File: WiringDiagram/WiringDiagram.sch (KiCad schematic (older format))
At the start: 0 parts

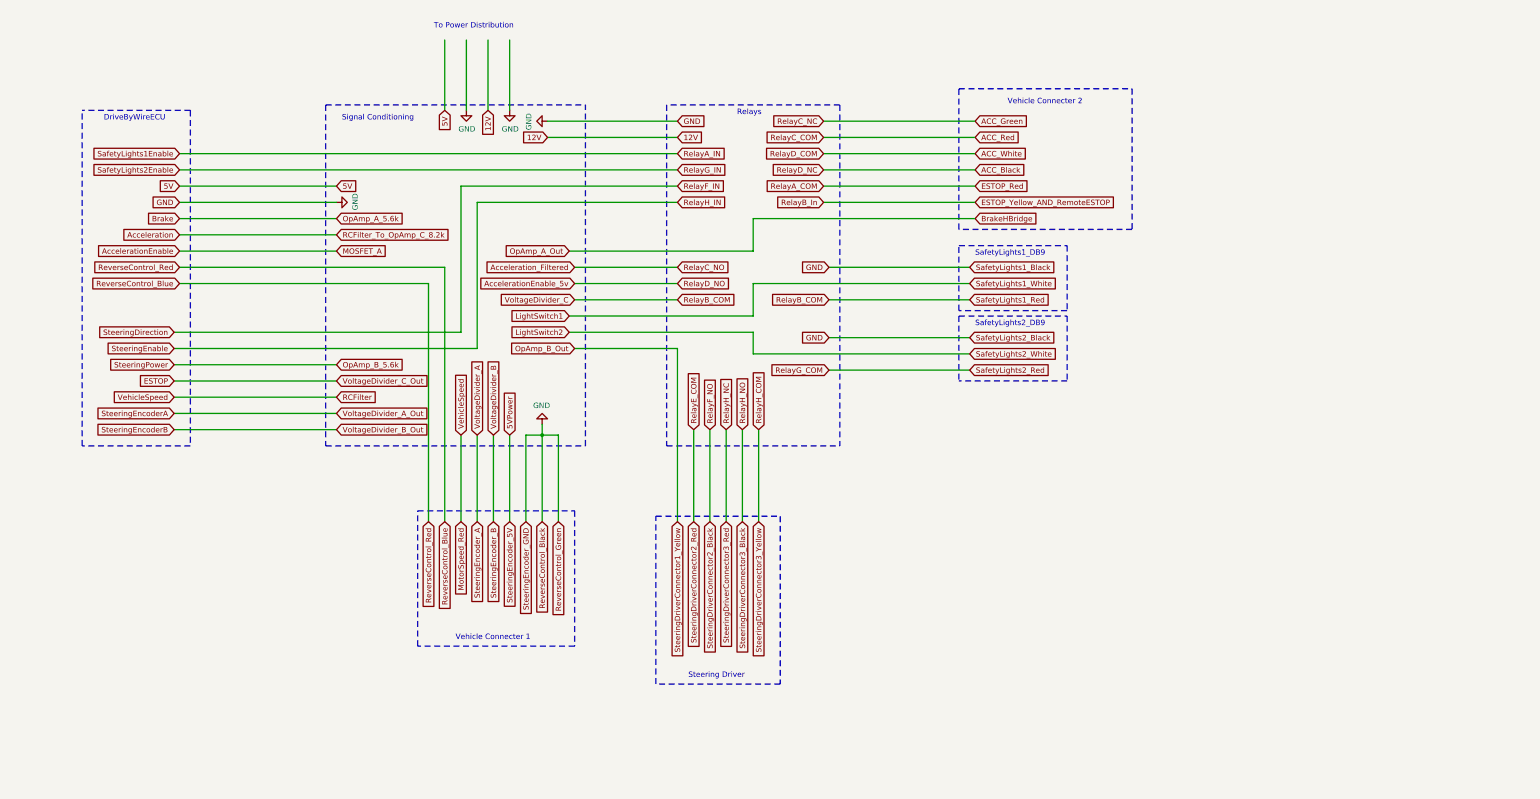
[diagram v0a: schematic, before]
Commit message: Finishes pinouts and moves them to the Wiring Daigram
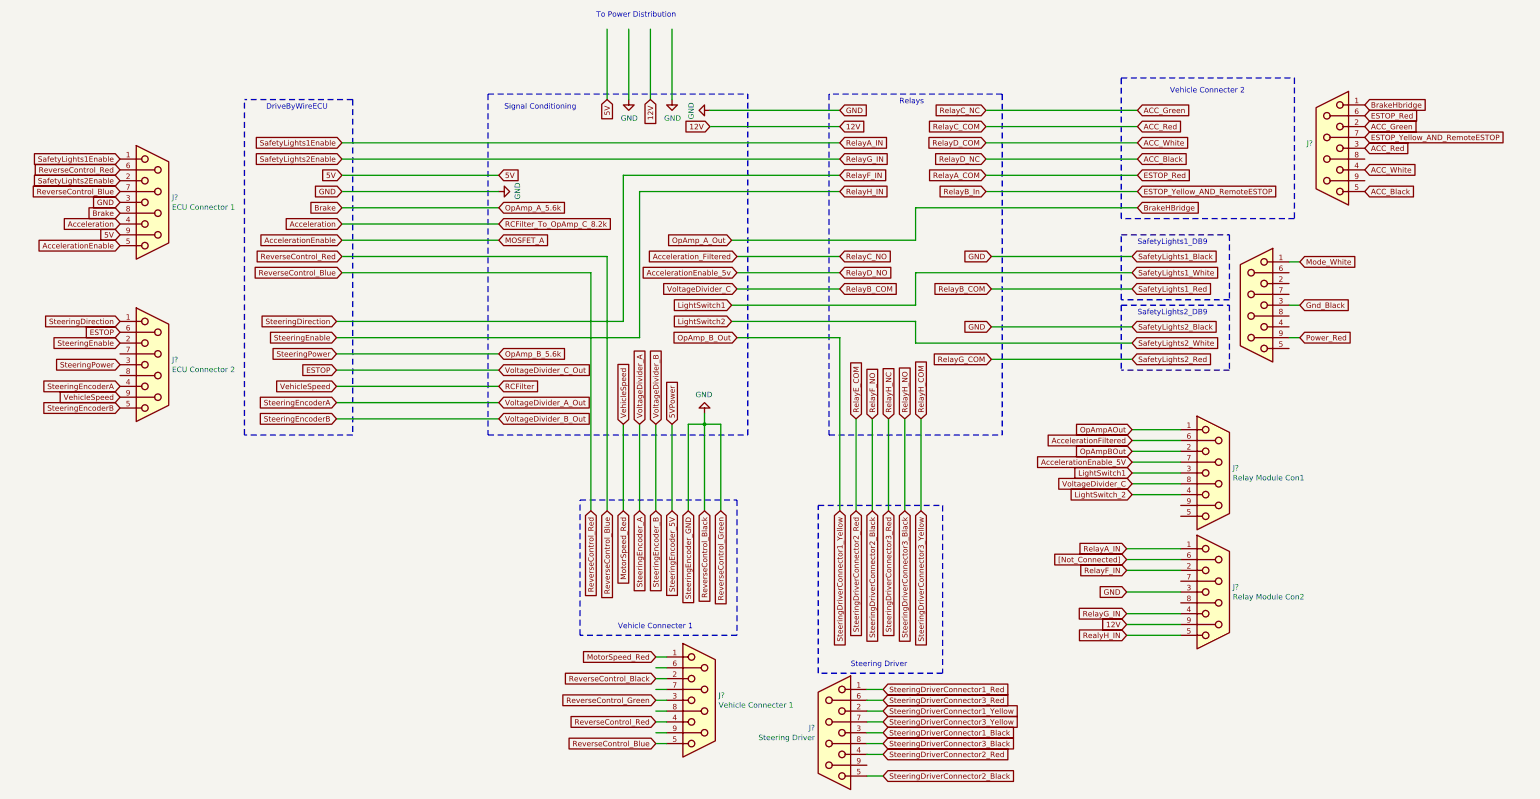
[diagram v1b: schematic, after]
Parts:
- added J1&?: SafetyLights, symbol Connector:DB9_Female
- added J?: Steering Driver, symbol Connector:DB9_Female
- added J?: Vehicle Connecter 1, symbol Connector:DB9_Female
- added J?: Relay Module Con2, symbol Connector:DB9_Female
- added J?: Relay Module Con1, symbol Connector:DB9_Female
- added J?: Vehicle Connnector 2, symbol Connector:DB9_Female
- added J?: ECU Connector 1, symbol Connector:DB9_Female
- added J?: ECU Connector 2, symbol Connector:DB9_Female
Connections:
- net labels added: AccelerationEnable_5V, AccelerationFiltered, BrakeHbridge, Gnd_Black, LightSwitch_2, Mode_White, OpAmpAOut, OpAmpBOut, Power_Red, RealyH_IN, SteeringDriverConnector1_Black, SteeringDriverConnector1_Red, [Not_Connected]
- wire segments 67 -> 101

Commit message: Encoder Pins Added to VC1 & VC2 Pins were rearranged
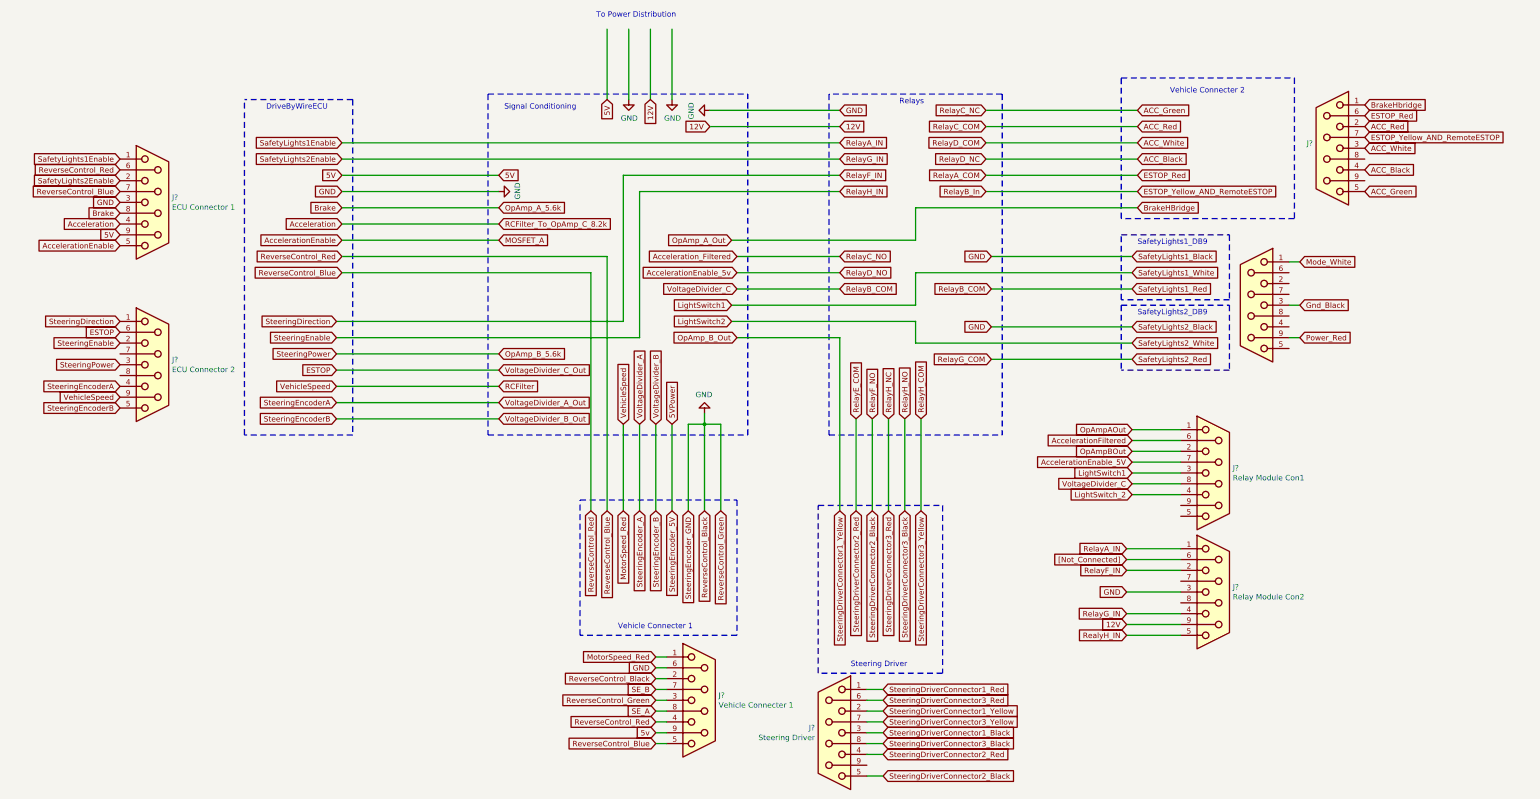
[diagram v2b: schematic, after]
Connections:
- net labels added: 5v, SE_A, SE_B
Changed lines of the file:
@@
 Wire Wire Line
 	7350 3650 8300 3650
-Text GLabel 11050 2450 2    50   Input ~ 0
-BrakeHBridge
 Text GLabel 7300 2750 0    50   Input ~ 0
 OpAmp_A_Out
@@
 Text GLabel 13150 1600 2    50   Input ~ 0
 ESTOP_Red
+Text GLabel 13150 2300 2    50   Input ~ 0
+ACC_Green
 Text GLabel 13150 1700 2    50   Input ~ 0
-ACC_Green
+ACC_Red
 Text GLabel 13150 1900 2    50   Input ~ 0
-ACC_Red
+ACC_White
 Text GLabel 13150 2100 2    50   Input ~ 0
-ACC_White
-Text GLabel 13150 2300 2    50   Input ~ 0
 ACC_Black
 Text GLabel 13150 1800 2    50   Input ~ 0
@@
 Text GLabel 1650 4200 0    50   Input ~ 0
 VehicleSpeed
+Text GLabel 11050 2450 2    50   Input ~ 0
+BrakeHBridge
+Text GLabel 6600 6700 0    50   Input ~ 0
+GND
+Text GLabel 6600 6900 0    50   Input ~ 0
+SE_B
+Text GLabel 6600 7100 0    50   Input ~ 0
+SE_A
+Text GLabel 6600 7300 0    50   Input ~ 0
+5v
 $EndSCHEMATC

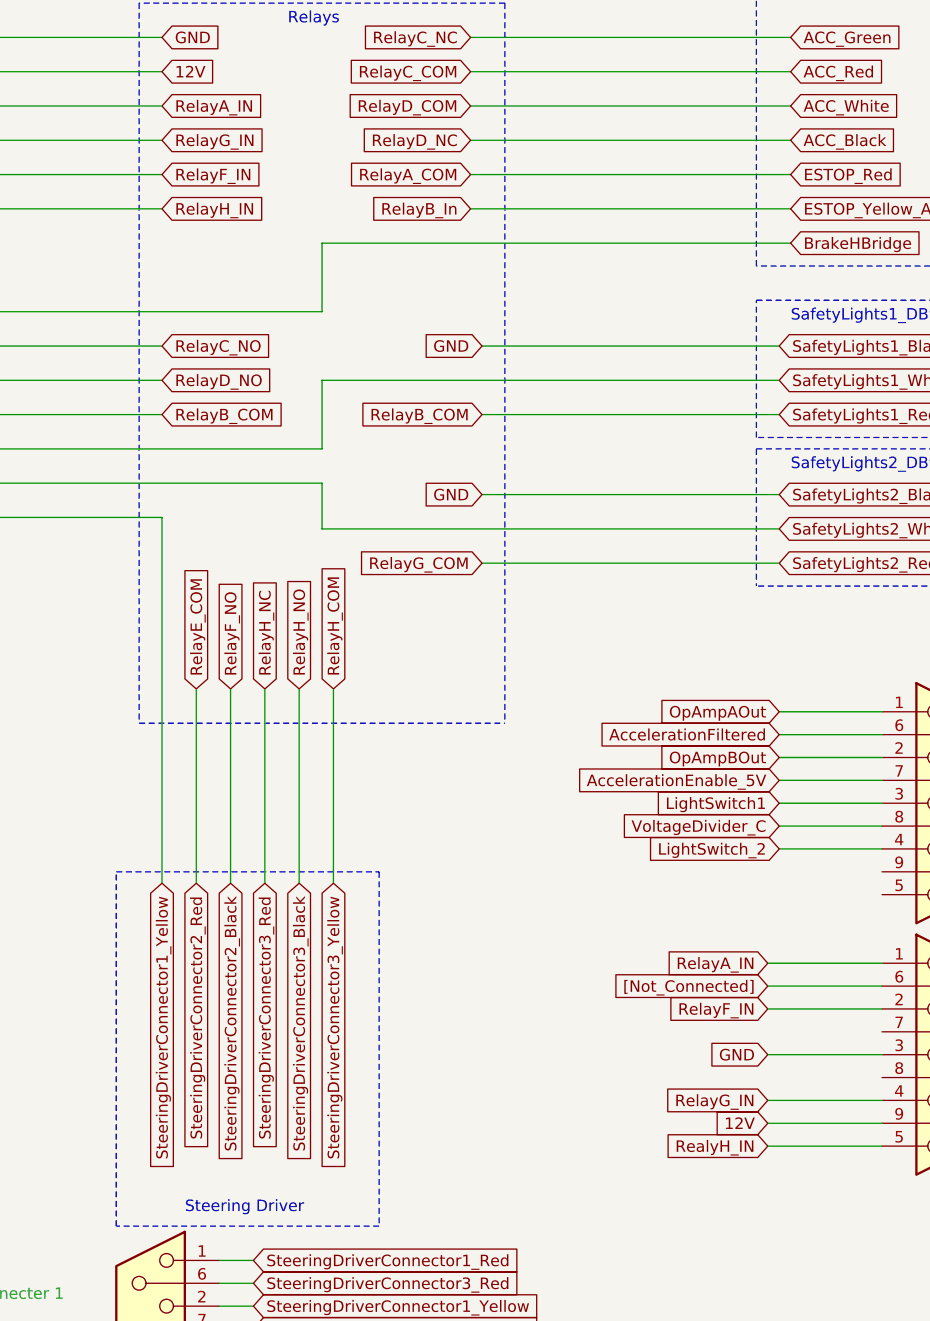
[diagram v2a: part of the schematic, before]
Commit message: Fixes relay wiring mismatch
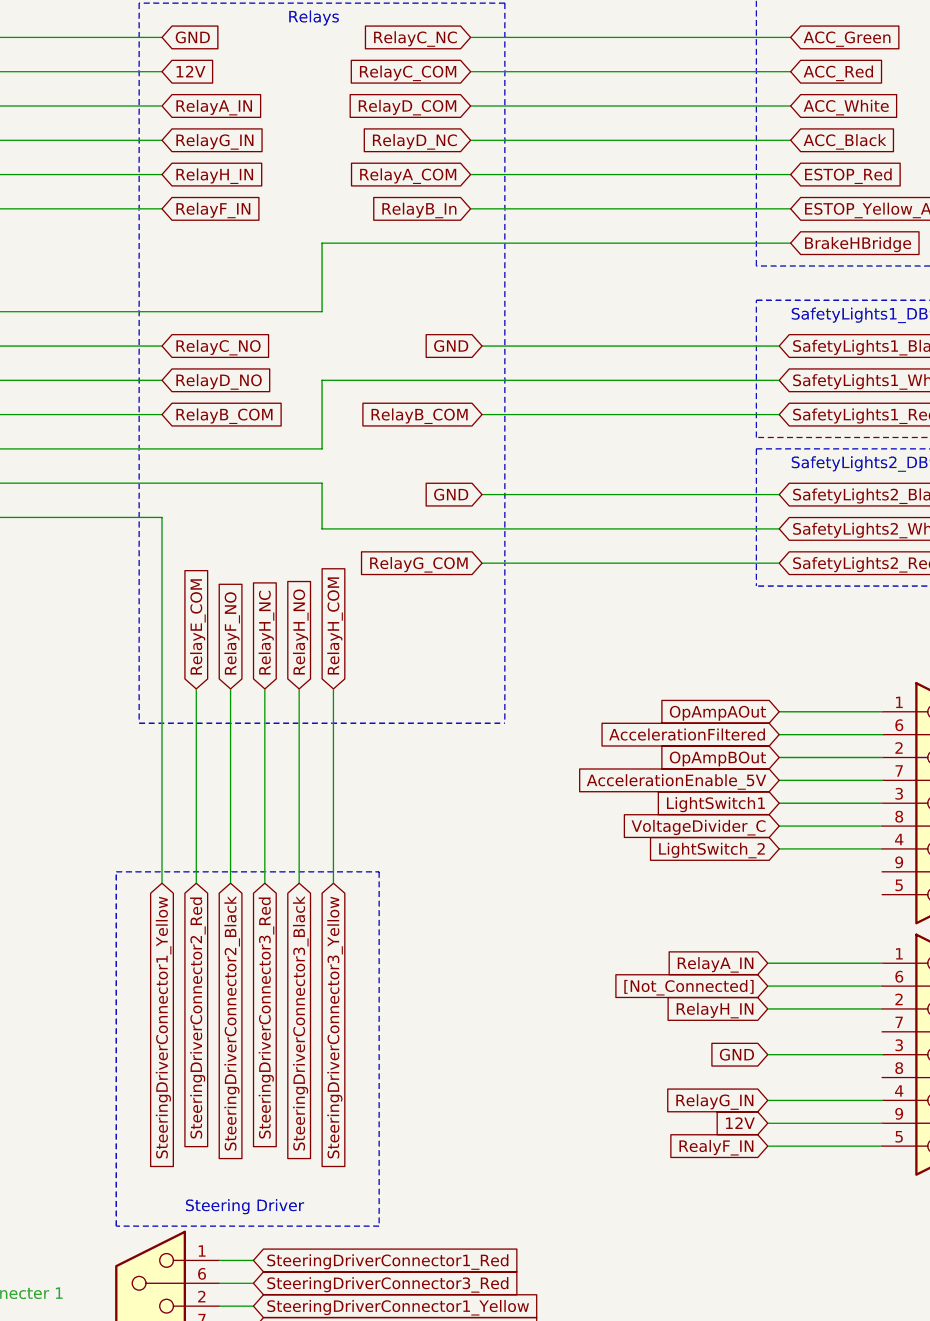
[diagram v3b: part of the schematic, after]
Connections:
- net labels added: RealyF_IN
- net labels removed: RealyH_IN
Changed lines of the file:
@@
 RelayB_COM
 Text GLabel 8300 2150 2    50   Input ~ 0
+RelayH_IN
+Text GLabel 8300 2300 2    50   Input ~ 0
 RelayF_IN
-Text GLabel 8300 2300 2    50   Input ~ 0
-RelayH_IN
 Wire Wire Line
 	6300 2150 8300 2150
@@
 $EndComp
 Text GLabel 10950 6400 0    50   Input ~ 0
-RealyH_IN
+RealyF_IN
 $Comp
 L Connector:DB9_Female J?
@@
 GND
 Text GLabel 10950 5800 0    50   Input ~ 0
-RelayF_IN
+RelayH_IN
 Text GLabel 10950 5600 0    50   Input ~ 0
 RelayA_IN
